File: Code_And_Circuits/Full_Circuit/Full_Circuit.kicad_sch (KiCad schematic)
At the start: 0 parts

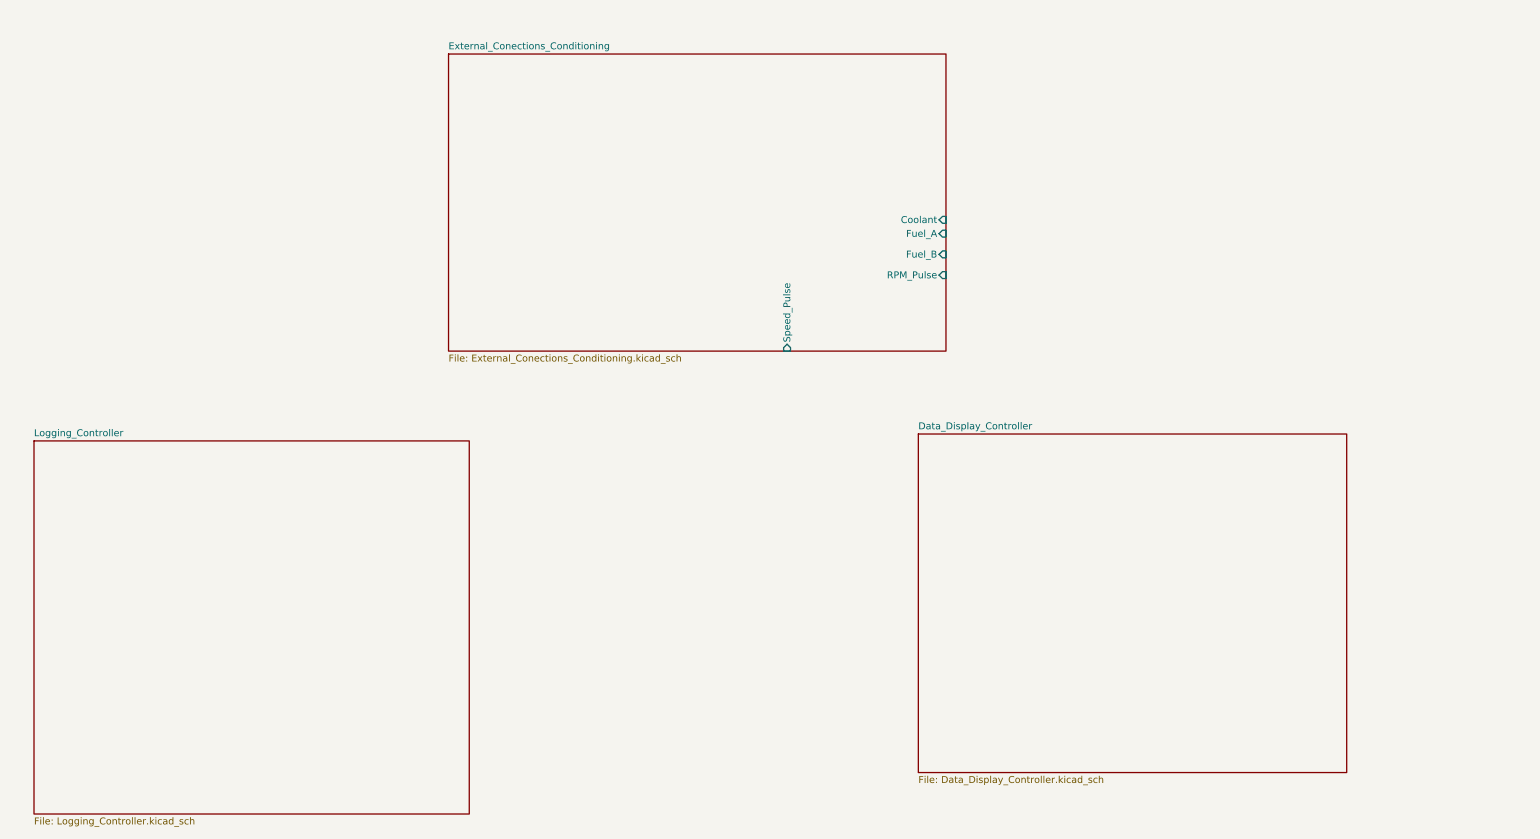
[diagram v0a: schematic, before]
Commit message: Finished schematic need to do PCB design and get Tachometer reference
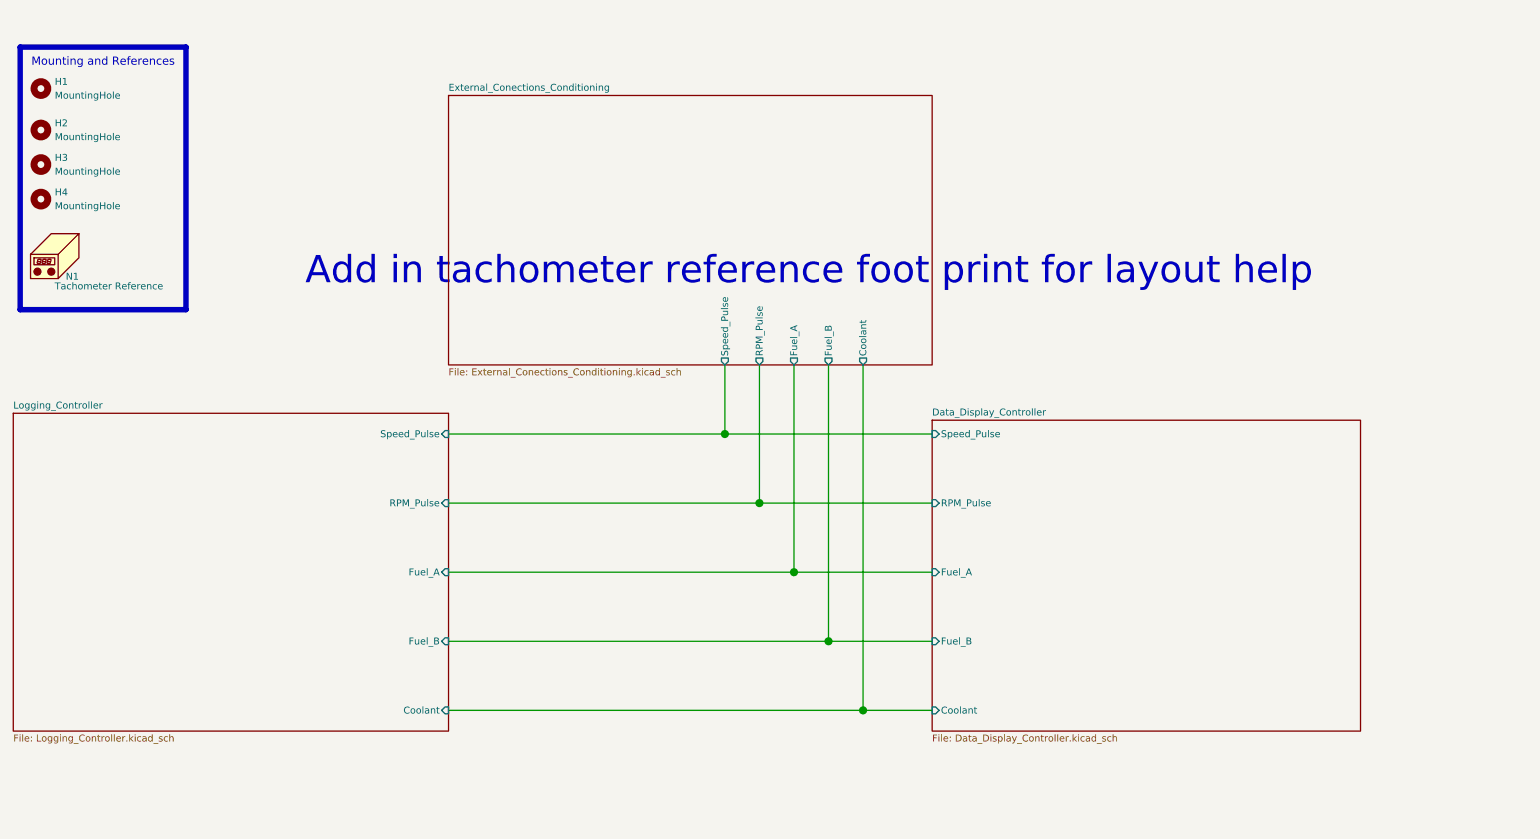
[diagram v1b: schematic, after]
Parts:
- added H1, H2, H3, H4: MountingHole, MountingHole:MountingHole_3.2mm_M3, symbol Mechanical:MountingHole
- added N1: Tachometer Reference, symbol Mechanical:Housing
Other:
- sheet Data_Display_Controller ports: added Coolant, Fuel_A, Fuel_B, RPM_Pulse, Speed_Pulse; removed none
- sheet Logging_Controller ports: added Coolant, Fuel_A, Fuel_B, RPM_Pulse, Speed_Pulse; removed none
- note added: "Add in tachometer reference foot print for layout help"
- note added: "Mounting and References"

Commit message: Reconfired some pin assignments for cleaner layout and adding reference footprints and mostly layed out board, due to space limits logging section has been ommitted
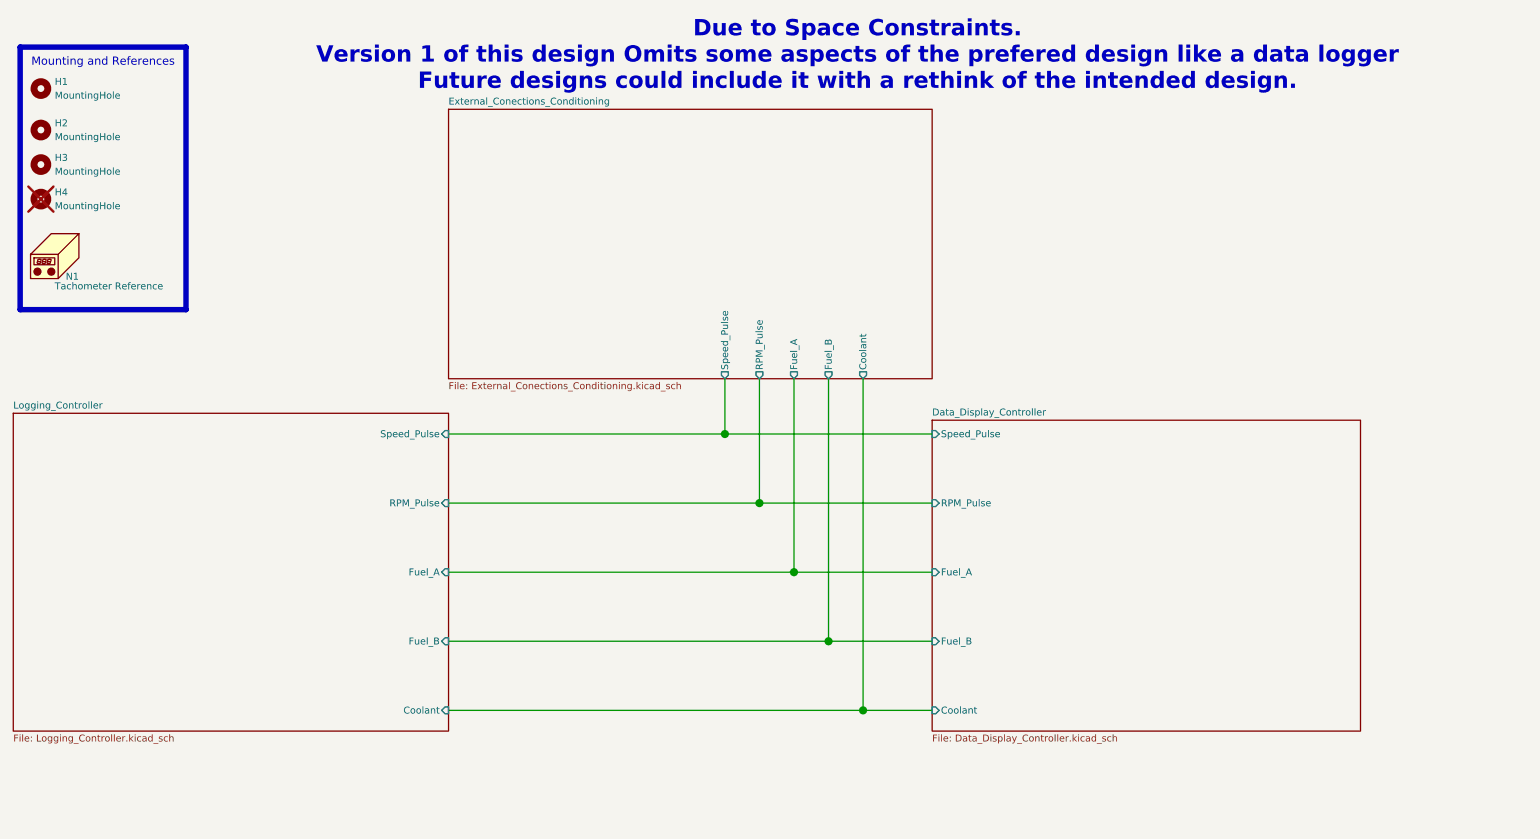
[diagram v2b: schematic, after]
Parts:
- H4: now not fitted
- N1: footprint (none) -> Added_Footprints:Dial_Gauge_Reference_CBF600
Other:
- note added: "Due to Space Constraints. Version 1 of this design Omits some aspects of the prefered design like a data logger Future designs could include it with a rethink of the intended design."
- note removed: "Add in tachometer reference foot print for layout help"
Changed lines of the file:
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@@
 		)
 	)
-	(text "Add in tachometer reference foot print for layout help"
-		(exclude_from_sim no)
-		(at 167.894 58.928 0)
+	(text "Due to Space Constraints.\nVersion 1 of this design Omits some aspects of the prefered design like a data logger\nFuture designs could include it with a rethink of the intended design."
+		(exclude_from_sim no)
+		(at 176.784 19.304 0)
 		(effects
 			(font
-				(size 5 5)
-				(color 0 0 255 1)
+				(size 3 3)
+				(thickness 0.6)
+				(bold yes)
+				(color 255 0 0 1)
 			)
 		)
@@
 	(wire
 		(pts
-			(xy 177.8 76.2) (xy 177.8 139.7)
+			(xy 177.8 78.74) (xy 177.8 139.7)
 		)
 		(stroke
@@
 	(wire
 		(pts
-			(xy 152.4 76.2) (xy 152.4 88.9)
+			(xy 152.4 78.74) (xy 152.4 88.9)
 		)
 		(stroke
@@
 	(wire
 		(pts
-			(xy 165.1 76.2) (xy 165.1 114.3)
+			(xy 165.1 78.74) (xy 165.1 114.3)
 		)
 		(stroke
@@
 	(wire
 		(pts
-			(xy 158.75 76.2) (xy 158.75 101.6)
+			(xy 158.75 78.74) (xy 158.75 101.6)
 		)
 		(stroke
@@
 	(wire
 		(pts
-			(xy 171.45 76.2) (xy 171.45 127)
+			(xy 171.45 78.74) (xy 171.45 127)
 		)
 		(stroke
@@
 			)
 		)
-		(property "Footprint" ""
+		(property "Footprint" "Added_Footprints:Dial_Gauge_Reference_CBF600"
 			(at 31.75 54.61 0)
 			(effects
@@
 		(exclude_from_sim no)
 		(in_bom no)
-		(on_board yes)
-		(dnp no)
+		(on_board no)
+		(dnp yes)
 		(fields_autoplaced yes)
 		(property "Reference" "H4"
@@
 	)
 	(sheet
-		(at 101.6 26.67)
+		(at 101.6 29.21)
 		(size 88.9 49.53)
 		(exclude_from_sim no)
@@
 		)
 		(property "Sheetname" "External_Conections_Conditioning"
-			(at 101.6 25.9584 0)
+			(at 101.6 28.4984 0)
 			(effects
 				(font
@@
 		)
 		(property "Sheetfile" "External_Conections_Conditioning.kicad_sch"
-			(at 101.6 76.7846 0)
+			(at 101.6 79.3246 0)
 			(effects
 				(font
@@
 		)
 		(pin "Coolant" output
-			(at 177.8 76.2 270)
+			(at 177.8 78.74 270)
 			(effects
 				(font
@@
 		)
 		(pin "Fuel_A" output
-			(at 165.1 76.2 270)
+			(at 165.1 78.74 270)
 			(effects
 				(font
@@
 		)
 		(pin "Fuel_B" output
-			(at 171.45 76.2 270)
+			(at 171.45 78.74 270)
 			(effects
 				(font
@@
 		)
 		(pin "RPM_Pulse" output
-			(at 158.75 76.2 270)
+			(at 158.75 78.74 270)
 			(effects
 				(font
@@
 		)
 		(pin "Speed_Pulse" output
-			(at 152.4 76.2 270)
-			(effects
-				(font
+			(at 152.4 78.74 270)
+			(effects
+				(font
